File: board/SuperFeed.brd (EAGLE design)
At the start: 97.8 x 59.7 mm, 16 parts

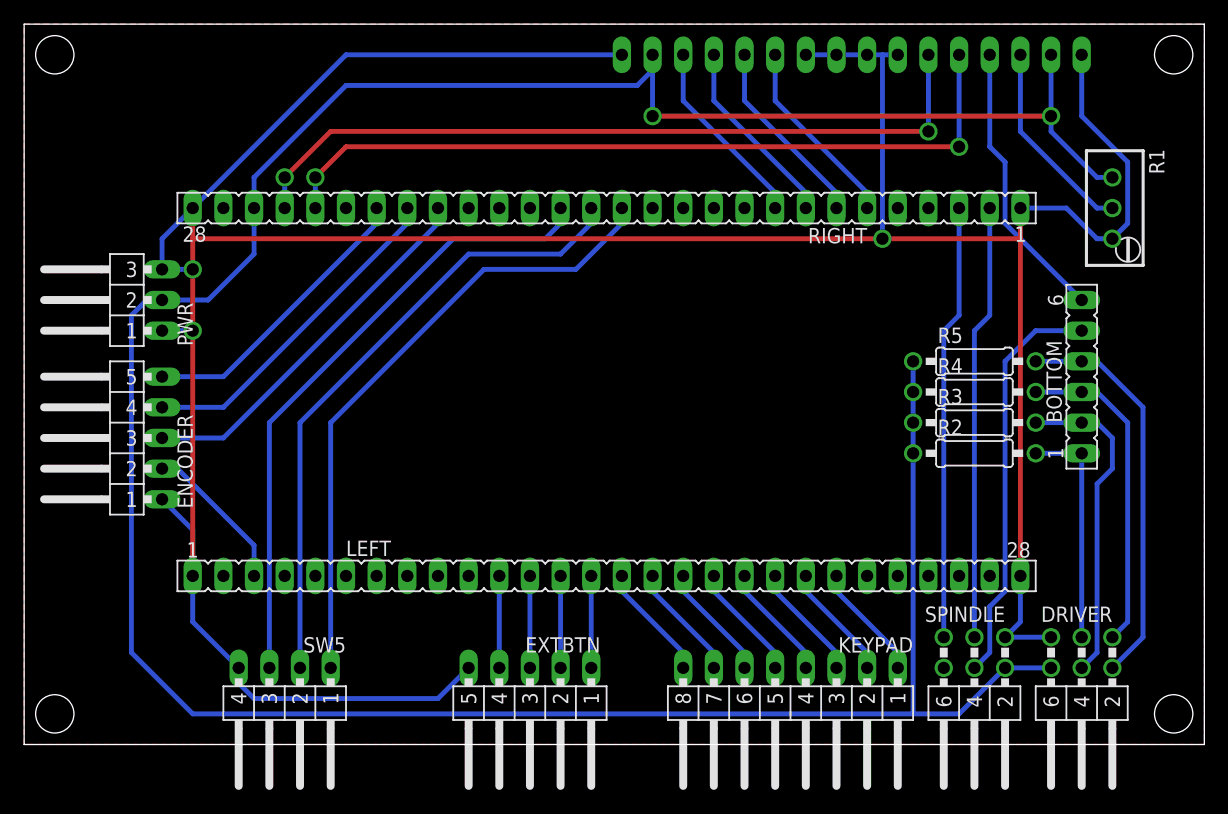
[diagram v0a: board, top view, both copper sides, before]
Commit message: Two more pins on extension connector
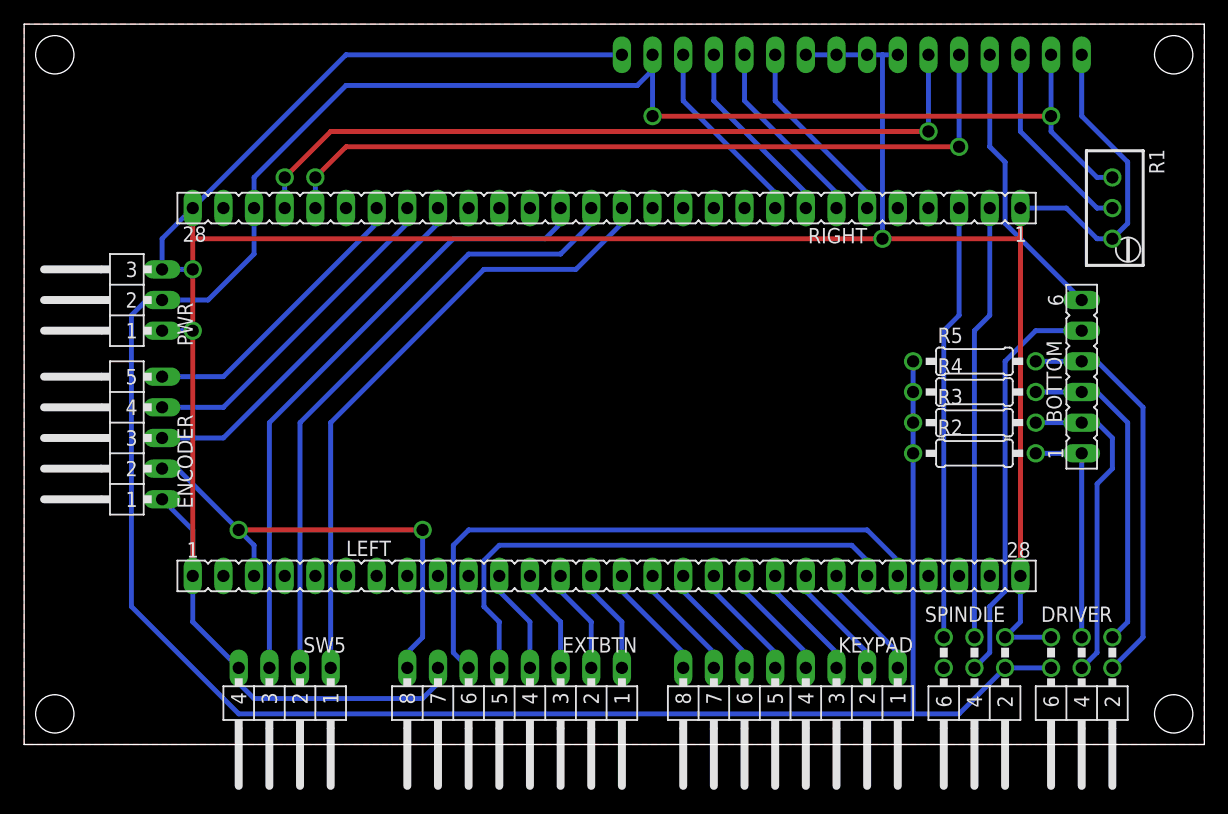
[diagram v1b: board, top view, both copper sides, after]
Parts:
- EXTBTN: device SuperFeed:MA05-1W -> SuperFeed:MA08-1W
- moved EXTBTN 1.27 mm to (40.6, 6.35)
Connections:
- net +3V3: now also EXTBTN.8
- net GND: now also EXTBTN.7; no longer EXTBTN.5
- net PC4: now also EXTBTN.5
- net PC5: now also EXTBTN.6
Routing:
- net PC5: track 0.00 -> 50.4 mm
- net PC4: track 0.00 -> 43.5 mm
- net +3V3: track 12.8 -> 40.0 mm, vias 0 -> 2
- net +5V: track 244.7 -> 242.5 mm
- net GND: track 279.6 -> 277.8 mm
- net PC1: track 7.62 -> 8.67 mm
- net PC3: track 7.62 -> 8.67 mm
- net PC2: track 7.62 -> 8.67 mm
- net PC0: track 7.62 -> 8.67 mm
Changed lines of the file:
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@@
 <element name="R4" library="SuperFeed" package="0207/10" value="10k" x="78.74" y="29.21"/>
 <element name="R5" library="SuperFeed" package="0207/10" value="10k" x="78.74" y="31.75"/>
-<element name="EXTBTN" library="SuperFeed" package="MA05-1W" value="" x="41.91" y="6.35" rot="R180"/>
+<element name="EXTBTN" library="SuperFeed" package="MA08-1W" value="" x="40.64" y="6.35" rot="R180"/>
 </elements>
 <signals>
@@
 <wire x1="13.97" y1="44.45" x2="13.97" y2="41.91" width="0.4064" layer="1"/>
 <contactref element="PWR" pad="1"/>
-<contactref element="EXTBTN" pad="5"/>
-<wire x1="34.29" y1="3.81" x2="36.83" y2="6.35" width="0.4064" layer="16"/>
-<wire x1="17.78" y1="6.35" x2="17.78" y2="5.08" width="0.4064" layer="16"/>
-<wire x1="17.78" y1="5.08" x2="19.05" y2="3.81" width="0.4064" layer="16"/>
-<wire x1="19.05" y1="3.81" x2="34.29" y2="3.81" width="0.4064" layer="16"/>
 <wire x1="11.43" y1="34.29" x2="13.97" y2="34.29" width="0.4064" layer="16"/>
 <via x="13.97" y="34.29" extent="1-16" drill="1.016"/>
@@
 <vertex x="0" y="59.69"/>
 </polygon>
+<contactref element="EXTBTN" pad="7"/>
+<wire x1="34.29" y1="6.35" x2="34.29" y2="5.08" width="0.4064" layer="16"/>
+<wire x1="34.29" y1="5.08" x2="33.02" y2="3.81" width="0.4064" layer="16"/>
+<wire x1="33.02" y1="3.81" x2="19.05" y2="3.81" width="0.4064" layer="16"/>
+<wire x1="19.05" y1="3.81" x2="17.78" y2="5.08" width="0.4064" layer="16"/>
+<wire x1="17.78" y1="5.08" x2="17.78" y2="6.35" width="0.4064" layer="16"/>
 </signal>
 <signal name="+5V">
@@
 <wire x1="11.43" y1="36.83" x2="10.16" y2="36.83" width="0.4064" layer="16"/>
 <wire x1="10.16" y1="36.83" x2="8.89" y2="35.56" width="0.4064" layer="16"/>
-<wire x1="8.89" y1="35.56" x2="8.89" y2="7.62" width="0.4064" layer="16"/>
-<wire x1="8.89" y1="7.62" x2="13.97" y2="2.54" width="0.4064" layer="16"/>
-<wire x1="13.97" y1="2.54" x2="73.66" y2="2.54" width="0.4064" layer="16"/>
 <wire x1="73.66" y1="2.54" x2="77.47" y2="2.54" width="0.4064" layer="16"/>
 <wire x1="19.05" y1="43.18" x2="19.05" y2="44.45" width="0.4064" layer="16"/>
@@
 <wire x1="15.24" y1="36.83" x2="19.05" y2="40.64" width="0.4064" layer="16"/>
 <wire x1="19.05" y1="40.64" x2="19.05" y2="44.45" width="0.4064" layer="16"/>
+<wire x1="73.66" y1="2.54" x2="17.78" y2="2.54" width="0.4064" layer="16"/>
+<wire x1="17.78" y1="2.54" x2="8.89" y2="11.43" width="0.4064" layer="16"/>
+<wire x1="8.89" y1="11.43" x2="8.89" y2="35.56" width="0.4064" layer="16"/>
 </signal>
 <signal name="NC">
@@
 <contactref element="ENCODER" pad="2"/>
 <wire x1="19.05" y1="13.97" x2="19.05" y2="16.51" width="0.4064" layer="16"/>
-<wire x1="19.05" y1="16.51" x2="12.7" y2="22.86" width="0.4064" layer="16"/>
+<wire x1="17.78" y1="17.78" x2="12.7" y2="22.86" width="0.4064" layer="16"/>
 <wire x1="12.7" y1="22.86" x2="11.43" y2="22.86" width="0.4064" layer="16"/>
+<contactref element="EXTBTN" pad="8"/>
+<wire x1="31.75" y1="6.35" x2="31.75" y2="7.62" width="0.4064" layer="16"/>
+<wire x1="31.75" y1="7.62" x2="33.02" y2="8.89" width="0.4064" layer="16"/>
+<wire x1="33.02" y1="8.89" x2="33.02" y2="17.78" width="0.4064" layer="16"/>
+<via x="33.02" y="17.78" extent="1-16" drill="1.016"/>
+<wire x1="33.02" y1="17.78" x2="17.78" y2="17.78" width="0.4064" layer="1"/>
+<via x="17.78" y="17.78" extent="1-16" drill="1.016"/>
+<wire x1="17.78" y1="17.78" x2="19.05" y2="16.51" width="0.4064" layer="16"/>
 </signal>
 <signal name="VBAT">
@@
 <signal name="PC4">
 <contactref element="LEFT" pad="23"/>
+<contactref element="EXTBTN" pad="5"/>
+<wire x1="39.37" y1="6.35" x2="39.37" y2="10.16" width="0.4064" layer="16"/>
+<wire x1="39.37" y1="10.16" x2="38.1" y2="11.43" width="0.4064" layer="16"/>
+<wire x1="38.1" y1="11.43" x2="38.1" y2="15.24" width="0.4064" layer="16"/>
+<wire x1="38.1" y1="15.24" x2="39.37" y2="16.51" width="0.4064" layer="16"/>
+<wire x1="39.37" y1="16.51" x2="68.58" y2="16.51" width="0.4064" layer="16"/>
+<wire x1="68.58" y1="16.51" x2="69.85" y2="15.24" width="0.4064" layer="16"/>
+<wire x1="69.85" y1="15.24" x2="69.85" y2="13.97" width="0.4064" layer="16"/>
 </signal>
 <signal name="PC5">
 <contactref element="LEFT" pad="24"/>
+<contactref element="EXTBTN" pad="6"/>
+<wire x1="72.39" y1="13.97" x2="72.39" y2="15.24" width="0.4064" layer="16"/>
+<wire x1="72.39" y1="15.24" x2="69.85" y2="17.78" width="0.4064" layer="16"/>
+<wire x1="69.85" y1="17.78" x2="36.83" y2="17.78" width="0.4064" layer="16"/>
+<wire x1="36.83" y1="17.78" x2="35.56" y2="16.51" width="0.4064" layer="16"/>
+<wire x1="35.56" y1="16.51" x2="35.56" y2="7.62" width="0.4064" layer="16"/>
+<wire x1="35.56" y1="7.62" x2="36.83" y2="6.35" width="0.4064" layer="16"/>
 </signal>
 <signal name="PB0">
@@
 <contactref element="LEFT" pad="14"/>
 <contactref element="EXTBTN" pad="1"/>
-<wire x1="46.99" y1="6.35" x2="46.99" y2="13.97" width="0.4064" layer="16"/>
+<wire x1="46.99" y1="13.97" x2="46.99" y2="12.7" width="0.4064" layer="16"/>
+<wire x1="46.99" y1="12.7" x2="49.53" y2="10.16" width="0.4064" layer="16"/>
+<wire x1="49.53" y1="10.16" x2="49.53" y2="6.35" width="0.4064" layer="16"/>
 </signal>
 <signal name="PC2">
 <contactref element="LEFT" pad="13"/>
 <contactref element="EXTBTN" pad="2"/>
-<wire x1="44.45" y1="13.97" x2="44.45" y2="6.35" width="0.4064" layer="16"/>
+<wire x1="44.45" y1="13.97" x2="44.45" y2="12.7" width="0.4064" layer="16"/>
+<wire x1="44.45" y1="12.7" x2="46.99" y2="10.16" width="0.4064" layer="16"/>
+<wire x1="46.99" y1="10.16" x2="46.99" y2="6.35" width="0.4064" layer="16"/>
 </signal>
 <signal name="PC1">
 <contactref element="LEFT" pad="12"/>
 <contactref element="EXTBTN" pad="3"/>
-<wire x1="41.91" y1="13.97" x2="41.91" y2="6.35" width="0.4064" layer="16"/>
+<wire x1="41.91" y1="13.97" x2="41.91" y2="12.7" width="0.4064" layer="16"/>
+<wire x1="41.91" y1="12.7" x2="44.45" y2="10.16" width="0.4064" layer="16"/>
+<wire x1="44.45" y1="10.16" x2="44.45" y2="6.35" width="0.4064" layer="16"/>
 </signal>
 <signal name="PC0">
 <contactref element="LEFT" pad="11"/>
 <contactref element="EXTBTN" pad="4"/>
-<wire x1="39.37" y1="13.97" x2="39.37" y2="6.35" width="0.4064" layer="16"/>
+<wire x1="39.37" y1="13.97" x2="39.37" y2="12.7" width="0.4064" layer="16"/>
+<wire x1="39.37" y1="12.7" x2="41.91" y2="10.16" width="0.4064" layer="16"/>
+<wire x1="41.91" y1="10.16" x2="41.91" y2="6.35" width="0.4064" layer="16"/>
 </signal>
 <signal name="PA1">

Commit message: Adjustments for better routing properties
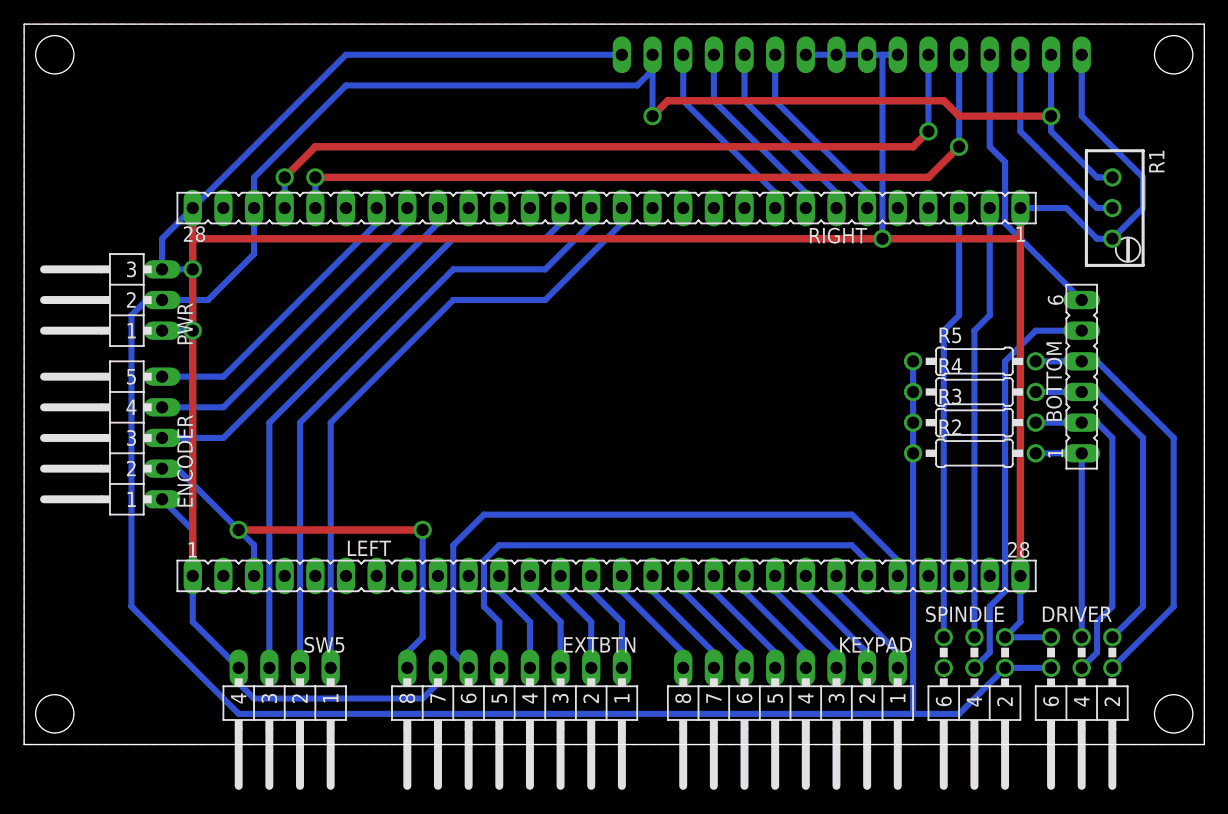
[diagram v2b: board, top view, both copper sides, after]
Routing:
- net PB13: track 33.1 -> 35.2 mm
- net PC5: track 50.4 -> 51.4 mm
- net +5V: track 242.5 -> 243.5 mm
- net PB12: track 27.0 -> 28.0 mm
- net GND: track 277.8 -> 278.9 mm
